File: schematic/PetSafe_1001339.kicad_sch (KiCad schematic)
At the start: 150 parts, among them J1 ICSP, J3 PIR BOARD, J5 MOTOR, J6 DNP, Q1 MMBT3904?, Q11 MMBTA55?, Q2 BC847B?, Q3 MMBTA55?, Q4 MMBTA55?, Q5 MMBTA55?, Q6 MMBTA55?, Q7 BC857C?, Q8 SIL3724A?, Q9 DNP, U1 S-1200B45?, U106 U6A / DNP, U2 SN74LVC2G14DBV?, U3 SGM8542XS, U4 PIC16F18855, U5 MX512H, U6 S-812C33AMC? / 3.3V, U7 DNP, Y1 20 MHz

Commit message: Distinguish logic and motor supplies and record VREF bias route
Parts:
- Q1: ViaEvidence v0.9.5: V011-V014 reach Q1.L and user reports VDD. Which VD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 -> v0.9.8: User explicitly confirms V011/V012/V013/V014 share 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
- R21, R23, R48: ViaEvidence (none) -> v0.9.8: User confirms V071-VREF. Earlier V071-R21.2 and V02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
- R22: ViaEvidence v0.9.3 V072 reaches TP6, explicitly not R22.2. Independent 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 -> v0.9.8: User confirms V071-VREF. Earlier V071-R21.2 and V02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
- TP103: value VDD / VDD pad -> VDD (logic supply); ViaEvidence (none) -> v0.9.8 follow-up: User confirms V082 reaches the board VDD 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
- TP104: ViaEvidence v0.9.8: Board silk VREF, native TP104. User confirms V026-VREF (PIC21/RB0) and explicitly rejects V053-VREF. Old RC1 photo association withdrawn. VREF is a board label, not an established voltage or IC function. -> v0.9.8: Board silk VREF, native TP104. User confirms V026-VREF (PIC21/RB0) and explicitly rejects V053-VREF. Old RC1 photo association withdrawn. VREF is a board label, not an established voltage or IC function. User also confirms V071/R21.2 to this VREF point; existing receiver-bias branches retain prior inference status.
- U4: ViaEvidence v0.9.8: User confirms RC2/PIC13-V049-TP3, RB0/PIC21-V026-VREF (native TP104), and RC1/PIC12-V053-V070-R18.1. User explicitly rejects V053-VREF, superseding the old photo assumption. No numerical resistance supplied for these connections. All PIC pads have modeled local destinations; other inferred branches still need review. RB4/PIC25-TP4 now also reaches V017/R42.1/R44.1. -> v0.9.8: User confirms RC2/PIC13-V049-TP3, RB0/PIC21-V026-VREF (native TP104), and RC1/PIC12-V053-V070-R18.1. User explicitly rejects V053-VREF, superseding the old photo assumption. No numerical resistance supplied for these connections. All PIC pads have modeled local destinations; other inferred branches still need review. RB4/PIC25-TP4 now also reaches V017/R42.1/R44.1. RB0/VREF also reaches V071/R21.2 by user report.
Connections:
- net H_RX_BIAS is gone; now on net PIC_RB0_VREF: R21.2, R22.2, R23.2, R48.2
- net H_VBAT: now also Q1.2 (E)
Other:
- note added: "Board VDD / TP103 = H_VDD logic rail -> U5 pin1 VCC. U5 pin4 VDD = H_VBAT motor rail."
- note added: "Q1.L -> V011-V014 -> motor H_VBAT / U5 pin4. Q1 identity/polarity still unverified."
- note added: "V082 -> H_VDD / TP103. D3 terminal unresolved; existing H_RX_VDD branch remains inferred."
- note added: "VDD / TP103: regulated logic supply H_VDD; candidate 4.5V, not measured. V082 confirmed here."
- note removed: "Q1.L -> V011-V014: user VDD. Rail choice pending; R43.2 -> TP14, separate from Q1.L."
- note removed: "U5 datasheet symbol: separate logic VCC and motor VDD; both ground pins retained."

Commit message: Separate battery and VSYS rails; confirm VREF and VDD via routes
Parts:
- removed Q1: MMBT3904?, Package_TO_SOT_SMD:SOT-23, symbol Transistor_BJT:MMBT3904
- added Q1: FMOS3401A?, Package_TO_SOT_SMD:SOT-23, symbol Transistor_FET:Q_PMOS_GSD
- C27: ViaEvidence v0.9: photo left pad/pin1 to V003/004 motor VDD (MX512H.4);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 -> v0.9.9: User corrects raw battery+ versus post-Q1 rail. BAT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
- C32: ViaEvidence (none) -> v0.9.9: V042 user-confirmed to board VDD test point TP103/V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
- C33, R3: ViaEvidence (none) -> v0.9.9: User corrects raw battery+ versus post-Q1 rail. BAT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
- C39: ViaEvidence (none) -> v0.9.9: User checked V035-VREF TP. Prior photo association 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
- L1, L2: ViaEvidence (none) -> v0.9.9: User confirms L1 and L2 connect to the same VSYS af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
- R21, R22, R23, R48: ViaEvidence v0.9.8: User confirms V071-VREF. Earlier V071-R21.2 and V026-VREF-PIC21/RB0 associations retained. R21.2 joins PIC_RB0_VREF. Existing R22.2/R23.2/R48.2 receiver-bias branches remain prior photo/circuit hypotheses, not new measured connections. VREF remains separate from H_VDD and RC1/V053. No voltage or numeric resistance supplied. -> v0.9.8: User confirms V071-VREF. Earlier V071-R21.2 and V026-VREF-PIC21/RB0 associations retained. R21.2 joins VREF. Existing R22.2/R23.2/R48.2 receiver-bias branches remain prior photo/circuit hypotheses, not new measured connections. VREF remains separate from VDD and RC1/V053. No voltage or numeric resistance supplied.
- R43, TP14: ViaEvidence v0.9.8: User confirms V015-TP14. Earlier V015-R43.2 lower-p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 -> v0.9.9: User corrects raw battery+ versus post-Q1 rail. BAT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
- R44: ViaEvidence v0.9.8: User confirms V017-TP4. Prior V017-R42.1/R44.1 loca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 -> v0.9.9: User corrects raw battery+ versus post-Q1 rail. BAT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
- TP101: value GND / GND pad -> GND
- TP103: value VDD (logic supply) -> VDD; ViaEvidence v0.9.8 follow-up: User confirms V082 reaches the board VDD 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 -> v0.9.9: User confirms V042 to this board VDD TP, matching t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
- TP104: ViaEvidence v0.9.8: Board silk VREF, native TP104. User confirms V026-V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 -> v0.9.9: User checked V035-VREF TP. Prior photo association 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
- TP107: value BATP / BATTERY + -> BATTERY (+); ViaEvidence (none) -> v0.9.9: User corrects raw battery+ versus post-Q1 rail. BAT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
- TP108: value BATN / BATTERY - -> BATTERY (-)
- U4: ViaEvidence v0.9.8: User confirms RC2/PIC13-V049-TP3, RB0/PIC21-V026-VR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 -> v0.9.9: User checked V035-VREF TP. Prior photo association 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
- U5: ViaEvidence v0.9.4: user confirms INA pin2 via V016-V022 to PIC15/RC4 a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 -> v0.9.9: User corrects raw battery+ versus post-Q1 rail. BAT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
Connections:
- net PIC_RB0_VREF is gone; now on net VREF: R21.2, R22.2, R23.2, R48.2, TP104.1, U4.21 (RB0)
- net at R44.2: now also Q1.1 (G)
- net BATTERY+: now reaches R43.2, TP14.1
- net BATTERY+: now also TP107.1, Q1.3 (D)
- net VREF: now reaches C39.1, U4.4 (RA2)
- net H_GND renamed GND
- net H_VBAT renamed VSYS
- net VSYS: now also Q1.2 (S); no longer TP107.1
- net H_VDD renamed VDD
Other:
- note added: "BATTERY+ -> Q1 -> VSYS / U5 pin4. Board VDD / TP103 = VDD -> U5 pin1."
- note added: "Q1: R1A -> FMOS3401A PMOS candidate. Battery+ at D3; post-Q1 supply at S2; G1 via R44."
- note added: "V082 -> VDD / TP103. D3 terminal unresolved; existing H_RX_VDD branch remains inferred."
- note added: "VDD / TP103: regulated logic supply VDD; candidate 4.5V, not measured. V082 confirmed here."
- note added: "v0.9.9 | KiCad 10.0.5 | 2026-10-08"
- note removed: "Board VDD / TP103 = H_VDD logic rail -> U5 pin1 VCC. U5 pin4 VDD = H_VBAT motor rail."
- note removed: "Q1.L -> V011-V014 -> motor H_VBAT / U5 pin4. Q1 identity/polarity still unverified."
- note removed: "V082 -> H_VDD / TP103. D3 terminal unresolved; existing H_RX_VDD branch remains inferred."
- note removed: "VDD / TP103: regulated logic supply H_VDD; candidate 4.5V, not measured. V082 confirmed here."
- note removed: "v0.9.8 | KiCad 10.0.5 | 2026-10-08"

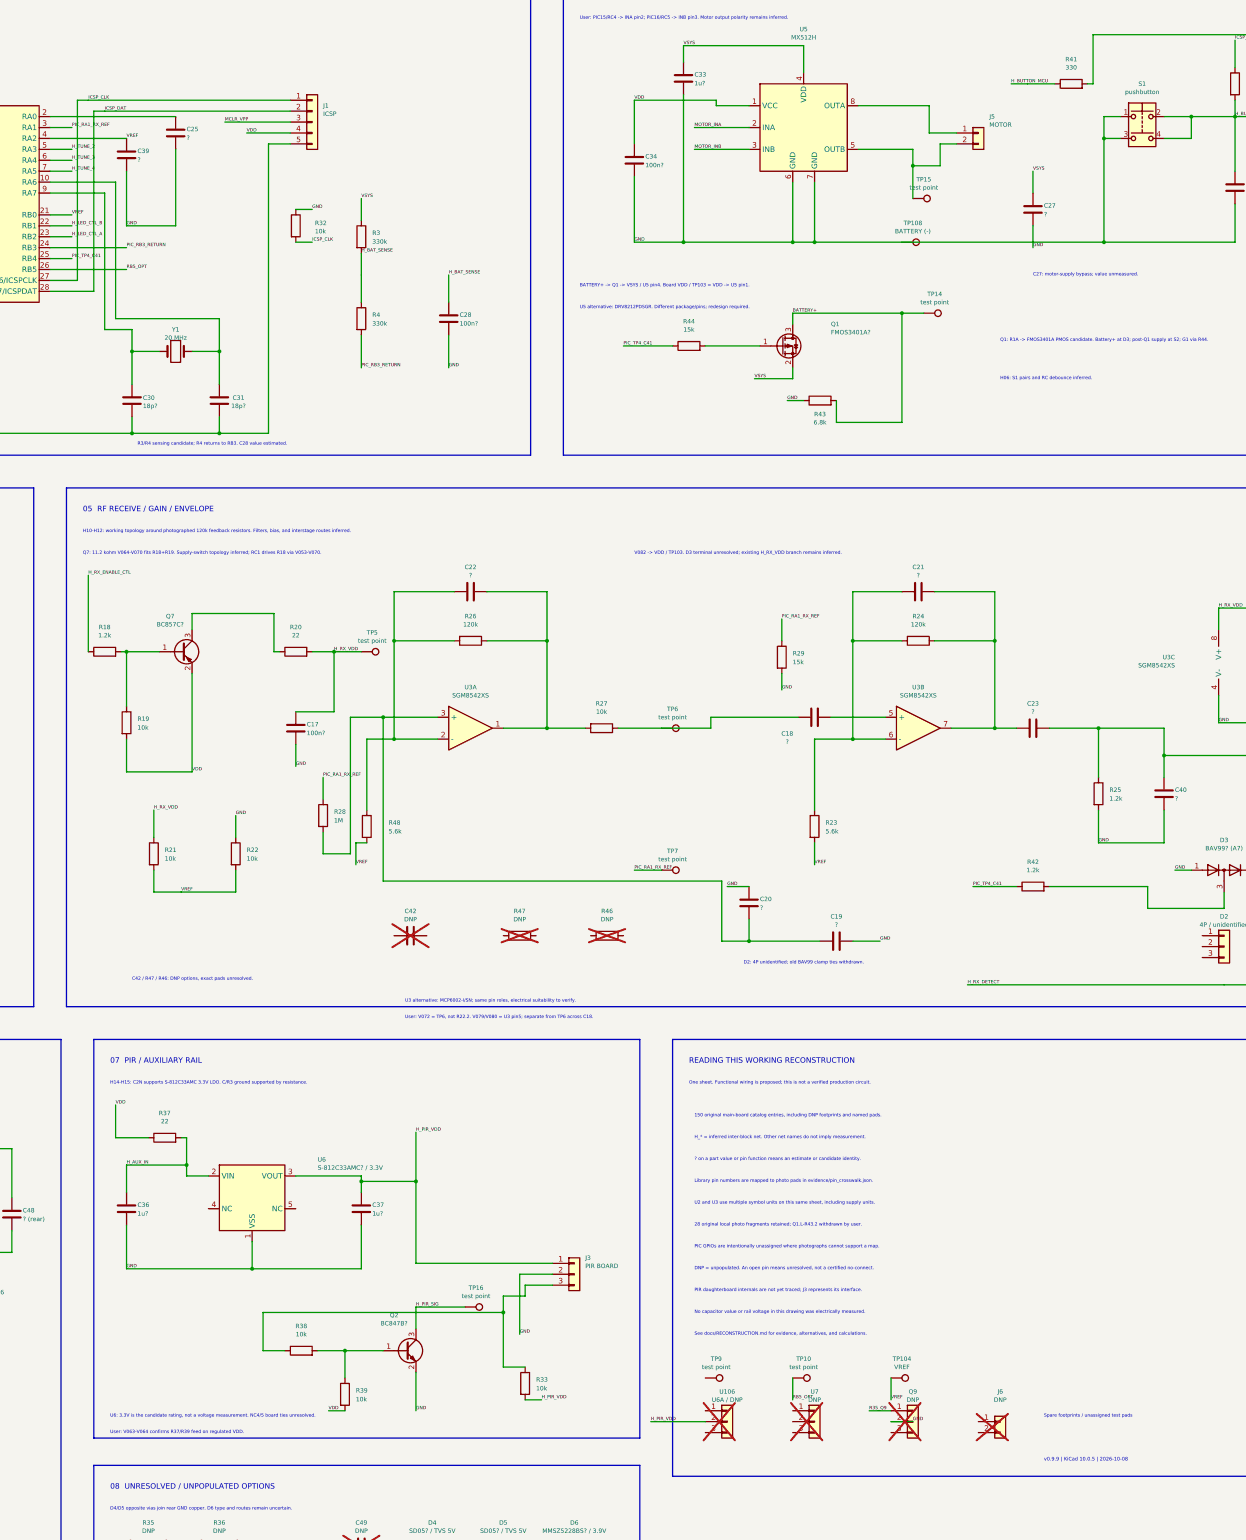
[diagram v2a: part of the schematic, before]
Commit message: Address architect review: J1 numbering, live completion checks and circuit gaps
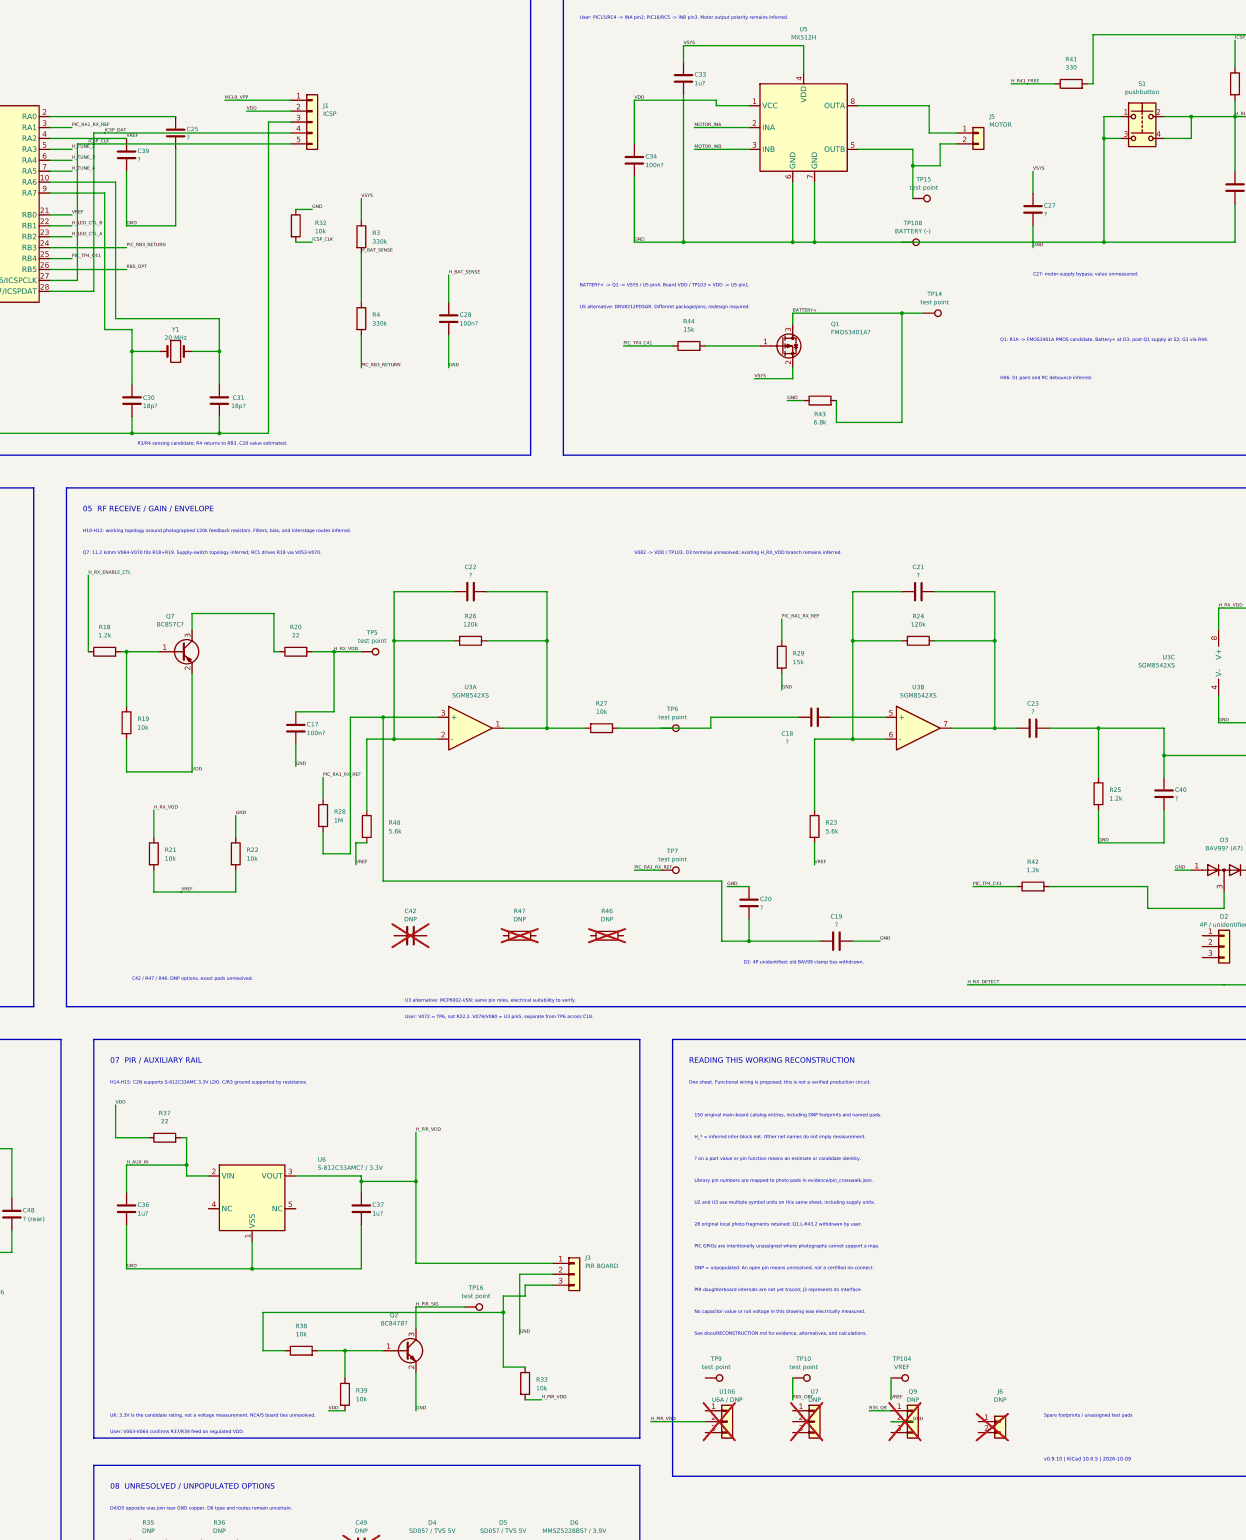
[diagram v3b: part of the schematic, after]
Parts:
- J1: FootprintBasis Five right-angle programming pins; compare spacing with adj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 -> Five right-angle 2.54 mm candidate header. Square pad1 corr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; PhysicalPinEvidence (none) -> IMG_2437 front: CLK-DAT-GND-VDD-VPP left to right; square p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; PinMapping See evidence/pin_crosswalk.json; physical orientation may b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 -> IMG_2437 front: CLK-DAT-GND-VDD-VPP left to right; square p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
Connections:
- net GND: now also J1.3 (Pin_3); no longer J1.5 (Pin_5)
- net ICSP_CLK: now also J1.5 (Pin_5); no longer J1.1 (Pin_1)
- net ICSP_DAT: now also J1.4 (Pin_4); no longer J1.2 (Pin_2)
- net MCLR_VPP: now also J1.1 (Pin_1); no longer J1.3 (Pin_3)
- net VDD: now also J1.2 (Pin_2); no longer J1.4 (Pin_4)
- net H_BUTTON_MCU renamed H_R41_FREE
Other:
- note added: "v0.9.10 | KiCad 10.0.5 | 2026-10-09"
- note removed: "v0.9.9 | KiCad 10.0.5 | 2026-10-08"
